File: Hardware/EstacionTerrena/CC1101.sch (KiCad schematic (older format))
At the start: 18 parts, among them U4 CC1101RGP, U5 0915BM15A0001E, Y2 26 MHz

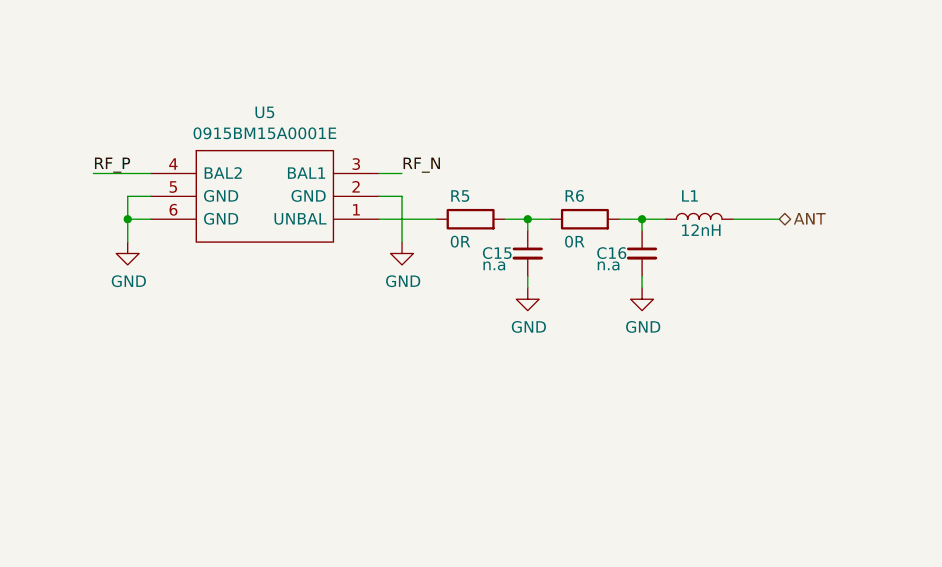
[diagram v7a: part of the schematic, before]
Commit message: Agregado a estación terrena el capacitor de bloqueo para el balun 885012005046
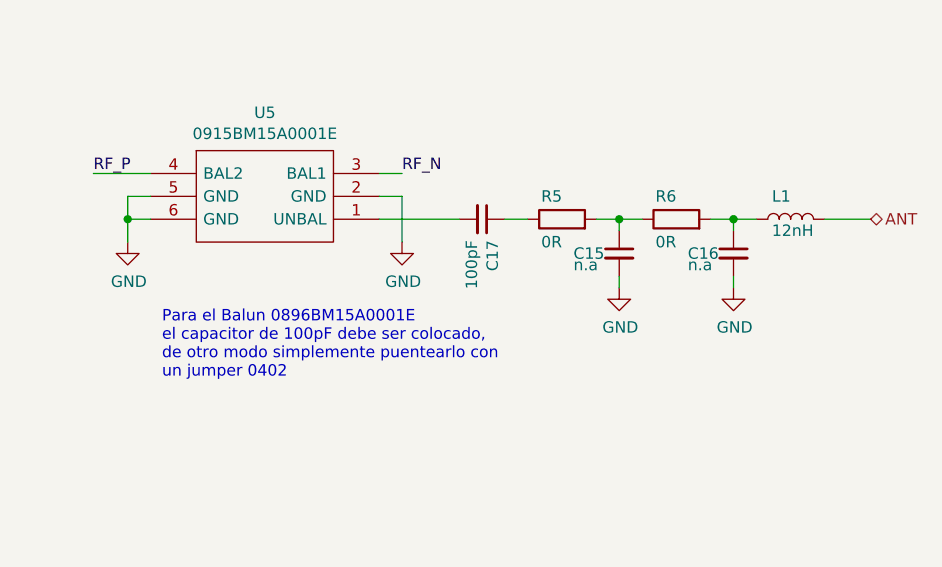
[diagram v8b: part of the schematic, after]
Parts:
- added C17: 100pF, Capacitor_SMD:C_0402_1005Metric, symbol Device:C_Small
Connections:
- net at R5.1: now also C17.1; no longer U5.1 (UNBAL)
- new net: C17.2, U5.1 (UNBAL)
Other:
- note added: "Para el Balun 0896BM15A0001E\nel capacitor de 100pF debe ser colocado,\nde otro modo simplemente puentearlo con\nun jumper 0402"
- moved on the sheet: C15, C16, L1, R5, R6
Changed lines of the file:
@@
 Text HLabel 2900 2300 0    50   Input ~ 0
 SI
-Text HLabel 9400 3500 2    50   BiDi ~ 0
+Text HLabel 9800 3500 2    50   BiDi ~ 0
 ANT
 $Bitmap
@@
 L Device:C_Small C15
 U 1 1 5B9B43C5
-P 8300 3650
-F 0 "C15" H 8100 3650 50  0000 L CNN
-F 1 "n.a" H 8100 3600 50  0000 L CNN
-F 2 "Capacitor_SMD:C_0402_1005Metric" H 8300 3650 50  0001 C CNN
-F 3 "~" H 8300 3650 50  0001 C CNN
-	1    8300 3650
+P 8700 3650
+F 0 "C15" H 8500 3650 50  0000 L CNN
+F 1 "n.a" H 8500 3600 50  0000 L CNN
+F 2 "Capacitor_SMD:C_0402_1005Metric" H 8700 3650 50  0001 C CNN
+F 3 "~" H 8700 3650 50  0001 C CNN
+	1    8700 3650
 	1    0    0    -1
 $EndComp
@@
 L Device:R R5
 U 1 1 5B9B44A8
-P 8050 3500
-F 0 "R5" V 8150 3500 50  0000 L CNN
-F 1 "0R" V 7950 3500 50  0000 L CNN
-F 2 "Resistor_SMD:R_0402_1005Metric" V 7980 3500 50  0001 C CNN
-F 3 "~" H 8050 3500 50  0001 C CNN
-F 4 "RC0402JR-070RL" V 8050 3500 50  0001 C CNN "Manufacturer Part Number"
-	1    8050 3500
+P 8450 3500
+F 0 "R5" V 8550 3500 50  0000 L CNN
+F 1 "0R" V 8350 3500 50  0000 L CNN
+F 2 "Resistor_SMD:R_0402_1005Metric" V 8380 3500 50  0001 C CNN
+F 3 "~" H 8450 3500 50  0001 C CNN
+F 4 "RC0402JR-070RL" V 8450 3500 50  0001 C CNN "Manufacturer Part Number"
+	1    8450 3500
 	0    -1   -1   0
 $EndComp
@@
 L Device:L L1
 U 1 1 5B9B4522
-P 9050 3500
-F 0 "L1" V 9150 3500 50  0000 L CNN
-F 1 "12nH" V 9000 3400 50  0000 L CNN
-F 2 "Inductor_SMD:L_0402_1005Metric" H 9050 3500 50  0001 C CNN
-F 3 "https://www.mouser.com/datasheet/2/611/jti-cat-rf-ind-844822.pdf" H 9050 3500 50  0001 C CNN
-F 4 "L-07C12NJV6" V 9050 3500 50  0001 C CNN "Manufacturer Part Number"
-	1    9050 3500
+P 9450 3500
+F 0 "L1" V 9550 3500 50  0000 L CNN
+F 1 "12nH" V 9400 3400 50  0000 L CNN
+F 2 "Inductor_SMD:L_0402_1005Metric" H 9450 3500 50  0001 C CNN
+F 3 "https://www.mouser.com/datasheet/2/611/jti-cat-rf-ind-844822.pdf" H 9450 3500 50  0001 C CNN
+F 4 "L-07C12NJV6" V 9450 3500 50  0001 C CNN "Manufacturer Part Number"
+	1    9450 3500
 	0    -1   -1   0
 $EndComp
@@
 L Device:C_Small C16
 U 1 1 5B9B73EA
-P 8800 3650
-F 0 "C16" H 8600 3650 50  0000 L CNN
-F 1 "n.a" H 8600 3600 50  0000 L CNN
-F 2 "Capacitor_SMD:C_0402_1005Metric" H 8800 3650 50  0001 C CNN
-F 3 "~" H 8800 3650 50  0001 C CNN
-	1    8800 3650
-	1    0    0    -1
-$EndComp
-Wire Wire Line
-	8200 3500 8300 3500
-Wire Wire Line
-	8300 3550 8300 3500
-Connection ~ 8300 3500
-Wire Wire Line
-	8300 3500 8400 3500
+P 9200 3650
+F 0 "C16" H 9000 3650 50  0000 L CNN
+F 1 "n.a" H 9000 3600 50  0000 L CNN
+F 2 "Capacitor_SMD:C_0402_1005Metric" H 9200 3650 50  0001 C CNN
+F 3 "~" H 9200 3650 50  0001 C CNN
+	1    9200 3650
+	1    0    0    -1
+$EndComp
+Wire Wire Line
+	8600 3500 8700 3500
+Wire Wire Line
+	8700 3550 8700 3500
+Connection ~ 8700 3500
 Wire Wire Line
 	8700 3500 8800 3500
 Wire Wire Line
-	8800 3550 8800 3500
-Connection ~ 8800 3500
-Wire Wire Line
-	8800 3500 8900 3500
-Wire Wire Line
-	7650 3500 7900 3500
+	9100 3500 9200 3500
+Wire Wire Line
+	9200 3550 9200 3500
+Connection ~ 9200 3500
+Wire Wire Line
+	9200 3500 9300 3500
 $Comp
 L power:GND #PWR041
 U 1 1 5B9C151D
-P 8300 3800
-F 0 "#PWR041" H 8300 3550 50  0001 C CNN
-F 1 "GND" H 8305 3627 50  0000 C CNN
-F 2 "" H 8300 3800 50  0001 C CNN
-F 3 "" H 8300 3800 50  0001 C CNN
-	1    8300 3800
+P 8700 3800
+F 0 "#PWR041" H 8700 3550 50  0001 C CNN
+F 1 "GND" H 8705 3627 50  0000 C CNN
+F 2 "" H 8700 3800 50  0001 C CNN
+F 3 "" H 8700 3800 50  0001 C CNN
+	1    8700 3800
 	1    0    0    -1
 $EndComp
@@
 L power:GND #PWR042
 U 1 1 5B9C1582
-P 8800 3800
-F 0 "#PWR042" H 8800 3550 50  0001 C CNN
-F 1 "GND" H 8805 3627 50  0000 C CNN
-F 2 "" H 8800 3800 50  0001 C CNN
-F 3 "" H 8800 3800 50  0001 C CNN
-	1    8800 3800
-	1    0    0    -1
-$EndComp
-Wire Wire Line
-	8300 3750 8300 3800
-Wire Wire Line
-	8800 3750 8800 3800
+P 9200 3800
+F 0 "#PWR042" H 9200 3550 50  0001 C CNN
+F 1 "GND" H 9205 3627 50  0000 C CNN
+F 2 "" H 9200 3800 50  0001 C CNN
+F 3 "" H 9200 3800 50  0001 C CNN
+	1    9200 3800
+	1    0    0    -1
+$EndComp
+Wire Wire Line
+	8700 3750 8700 3800
+Wire Wire Line
+	9200 3750 9200 3800
 Wire Wire Line
 	7650 3400 7750 3400
@@
 	7750 3400 7750 3600
 Wire Wire Line
-	9200 3500 9400 3500
+	9600 3500 9800 3500
 Wire Wire Line
 	2900 3250 2700 3250
@@
 L Device:R R6
 U 1 1 5BF0F124
-P 8550 3500
-F 0 "R6" V 8650 3500 50  0000 L CNN
-F 1 "0R" V 8450 3500 50  0000 L CNN
-F 2 "Resistor_SMD:R_0402_1005Metric" V 8480 3500 50  0001 C CNN
-F 3 "~" H 8550 3500 50  0001 C CNN
-F 4 "RC0402JR-070RL" V 8550 3500 50  0001 C CNN "Manufacturer Part Number"
-	1    8550 3500
+P 8950 3500
+F 0 "R6" V 9050 3500 50  0000 L CNN
+F 1 "0R" V 8850 3500 50  0000 L CNN
+F 2 "Resistor_SMD:R_0402_1005Metric" V 8880 3500 50  0001 C CNN
+F 3 "~" H 8950 3500 50  0001 C CNN
+F 4 "RC0402JR-070RL" V 8950 3500 50  0001 C CNN "Manufacturer Part Number"
+	1    8950 3500
 	0    -1   -1   0
 $EndComp
@@
 	1    0    0    -1
 $EndComp
+Text Notes 6700 4200 0    50   ~ 0
+Para el Balun 0896BM15A0001E\nel capacitor de 100pF debe ser colocado,\nde otro modo simplemente puentearlo con\nun jumper 0402
+$Comp
+L Device:C_Small C?
+U 1 1 5C25BE51
+P 8100 3500
+AR Path="/5B9997DB/5C25BE51" Ref="C?"  Part="1"
+AR Path="/5B9A8077/5C25BE51" Ref="C17"  Part="1"
+F 0 "C17" H 8192 3546 50  0000 L CNN
+F 1 "100pF" H 8192 3455 50  0000 L CNN
+F 2 "Capacitor_SMD:C_0402_1005Metric" H 8100 3500 50  0001 C CNN
+F 3 "~" H 8100 3500 50  0001 C CNN
+F 4 "NP0" H 8100 3500 50  0001 C CNN "Dielectric"
+F 5 "25V" H 8100 3500 50  0001 C CNN "Voltage"
+F 6 "885012005046" H 8100 3500 50  0001 C CNN "Manufacturer Part Number"
+	1    8100 3500
+	0    1    1    0
+$EndComp
+Wire Wire Line
+	7650 3500 8000 3500
+Wire Wire Line
+	8200 3500 8300 3500
 $EndSCHEMATC
